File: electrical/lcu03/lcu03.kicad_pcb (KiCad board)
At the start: 2 copper layers, 99.5 x 50 mm, 121 parts, among them P1 screw, P10 swd, P11 stepper_conn, P12 stepper_conn, P13 stepper_conn, P14 stepper_conn, P15 stepper_conn, P16 screw, P17 screw, P2 screw, P3 screw, P4 screw, P5 ext-1, P6 ~rst~, P7 mode, P8 ext-2, P9 USB_B, Q1 bc857, Q2 bc847, Q3 bc857, Q4 ntd18n06l, U1 crystal-4pin, U2 CP2102, U3 m24c02, U4 NCP3063, U5 MCP1703T-3302E/CB, U6 ts881, U7 lb1930mc, U8 a4985, U9 a4985

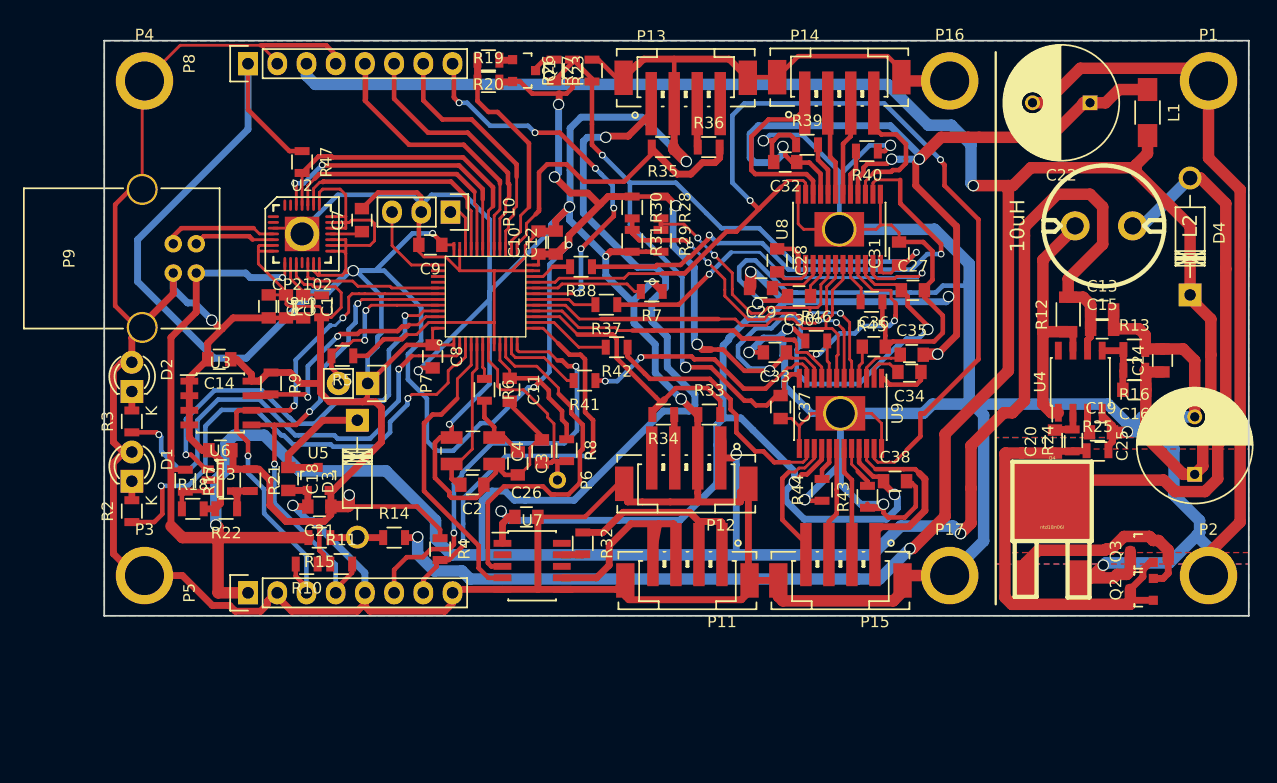
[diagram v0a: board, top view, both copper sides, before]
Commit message: Replaced linear regulator, changed socket footprints and implemented all improvements from "zzz.txt" file.
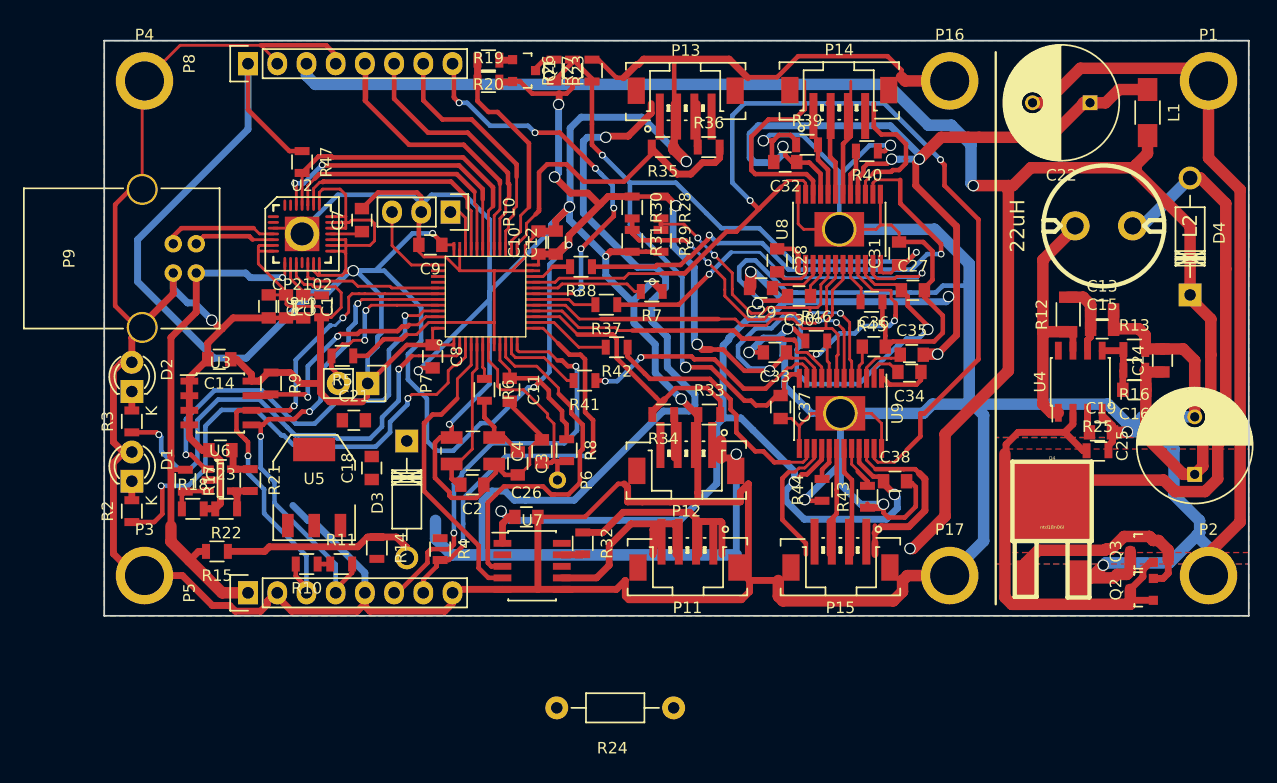
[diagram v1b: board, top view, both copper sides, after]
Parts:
- removed C20: 10n, Capacitors_SMD:C_0805
- C19: value 1n2 -> 2n4
- L2: value 10uH -> 22uH
- P11, P12, P13, P14, P15: footprint my-lib:JST_B4B-PH-SM4-TB -> my-lib:my-JST_B4B-PH-SM4-TB
- R14, R15: value 0 -> ferrite bead
- R24: value 470 5% -> 10 5%; footprint Resistors_SMD:R_0805 -> Resistors_ThroughHole:Resistor_Horizontal_RM10mm
- R32: value 10 5% -> 0
- U5: value MCP1703T-3302E/CB -> my-NCP1117ST50T3G; footprint TO_SOT_Packages_SMD:SOT-23 -> TO_SOT_Packages_SMD:SOT-223
- moved R24 41.7 mm to (137.5, 129.0), turned to 180 degrees
- moved R15 8.98 mm to (97.8, 115.4)
- moved C21 8.08 mm to (109.7, 104.0), turned to 0 degrees
- moved C18 7.31 mm to (111.2, 108.2), turned to 90 degrees
- moved D3 4.66 mm to (114.3, 105.8)
- moved R14 1.75 mm to (111.7, 115.1), turned to 270 degrees
- moved U5 0.83 mm to (106.2, 109.8)
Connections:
- Q2 pad 1: Net-(C20-Pad1) -> Net-(Q2-Pad1)
- Q2 pad 3: Net-(C20-Pad1) -> Net-(Q2-Pad1)
- Q3 pad 1: Net-(C20-Pad1) -> Net-(Q2-Pad1)
- R24 pad 1: Net-(C20-Pad1) -> Net-(P11-Pad1)
- R24 pad 2: Net-(C20-Pad2) -> /shutter-out-a
- R25 pad 1: Net-(C20-Pad1) -> Net-(Q2-Pad1)
- U4 pad 2: Net-(C20-Pad2) -> Net-(Q2-Pad1)
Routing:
- net /Vbus: track 266.3 -> 53.7 mm, vias 5 -> 1
- net GND: track 834.7 -> 936.9 mm, vias 18 -> 19
- net /reg-fb: track 210.2 -> 162.8 mm, vias 3 -> 2
- net VDD: track 373.9 -> 332.8 mm, vias 11 -> 10
- net Net-(Q2-Pad1): track 0.00 -> 41.1 mm
- net Net-(C20-Pad1): track 37.5 -> 0.00 mm
- net Net-(D3-Pad2): track 4.63 -> 17.4 mm
- net Net-(C18-Pad1): track 10.9 -> 0.00 mm
- net Net-(C20-Pad2): track 3.00 -> 0.00 mm
- net /tx-2: track 38.0 -> 37.4 mm

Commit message: Finished routing. Going to apply a few beautifications.
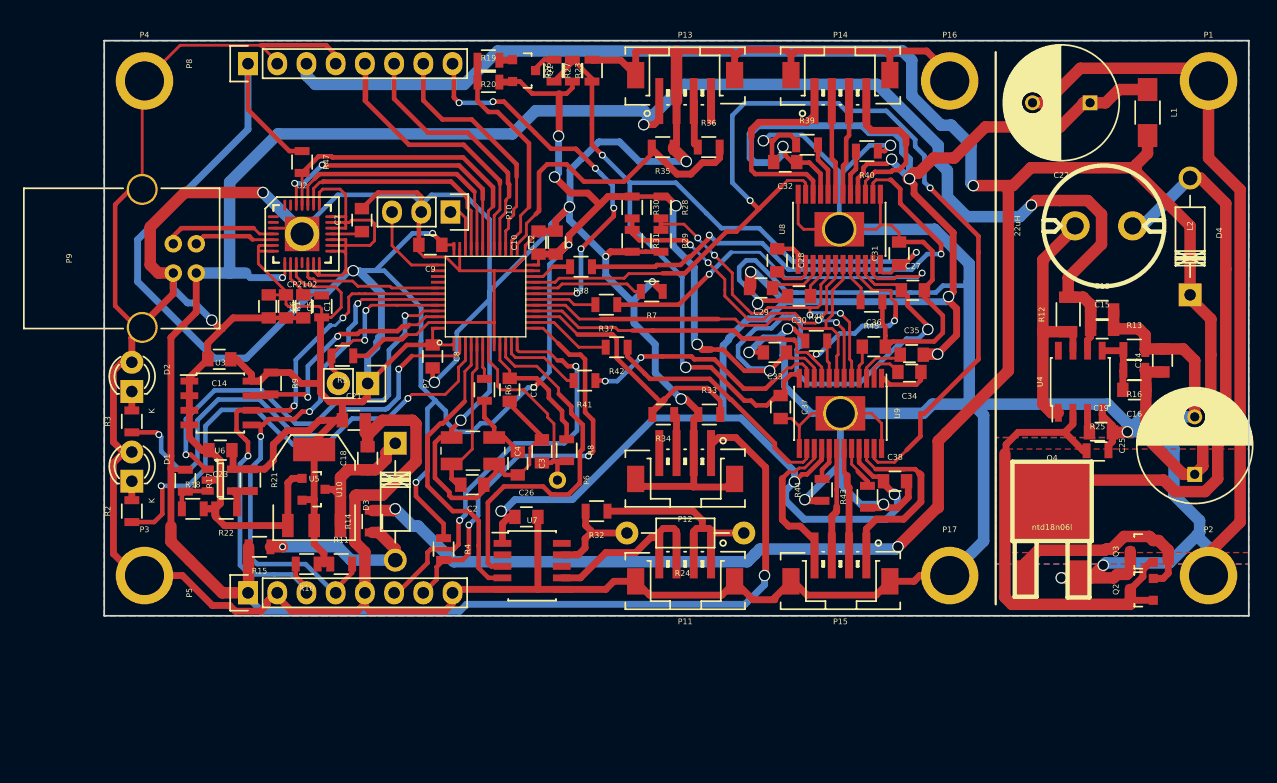
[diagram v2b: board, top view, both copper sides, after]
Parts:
- added U10: MCP1703T-3302E/CB, TO_SOT_Packages_SMD:SOT-23, F.Cu at (106.2, 110.0)
- moved R24 16.4 mm to (143.6, 113.8)
- moved R15 3.72 mm to (101.5, 115.0)
- moved R32 3.05 mm to (130.8, 111.9), turned to 180 degrees
- moved R14 2.33 mm to (111.3, 112.8), turned to 90 degrees
- moved P13 1.35 mm to (138.5, 74.0)
- moved P14 1.30 mm to (152.0, 74.0)
- moved P11 1.22 mm to (138.5, 118.0)
- moved P15 1.20 mm to (152.0, 118.0)
- moved D3 1.02 mm to (113.3, 106.0)
- moved C18 0.92 mm to (110.9, 107.3)
- moved P12 0.71 mm to (138.5, 109.1)
- moved R4 0.30 mm to (117.5, 115.2)
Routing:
- net /Vbus: track 53.7 -> 228.8 mm, vias 1 -> 4
- net GND: track 936.9 -> 859.7 mm
- net /reg-fb: track 162.8 -> 215.4 mm, vias 2 -> 3
- net VDD: track 332.8 -> 381.9 mm, vias 10 -> 11
- net Net-(C18-Pad1): track 0.00 -> 14.6 mm
- net /shutter-out-a: track 1.84 -> 9.00 mm
- net /stepper-subcircuit-2/out1b: track 11.8 -> 16.4 mm
- net /i2c1-sda: track 44.2 -> 47.5 mm
- net /shutter-out-b: track 21.0 -> 18.0 mm
- net /stepper-subcircuit-1/Vbb: track 180.1 -> 177.3 mm
- net /i2c1-scl: track 45.9 -> 48.7 mm
- net /stepper-subcircuit-2/out2a: track 12.1 -> 9.48 mm
- net /stepper-subcircuit-1/out1a: track 10.9 -> 8.32 mm
- net /stepper-subcircuit-2/out2b: track 20.2 -> 17.7 mm
- net Net-(D3-Pad2): track 17.4 -> 14.9 mm, vias 0 -> 1
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
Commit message: Finished beautifications. Generated gerber files.
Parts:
- moved C13 0.55 mm to (174.8, 93.9)
- moved C16 0.35 mm to (177.6, 101.7)
- moved R13 0.25 mm to (177.6, 97.6)
- moved C15 0.16 mm to (174.8, 95.9)
- moved R16 0.07 mm to (177.6, 99.7)
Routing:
- net VDD: track 381.9 -> 406.5 mm, vias 11 -> 10
- net GND: track 859.7 -> 869.6 mm, vias 19 -> 21
- net /Vbus: track 228.8 -> 223.6 mm
- net /stepper-subcircuit-1/Vbb: track 177.3 -> 180.9 mm, vias 9 -> 8
- net /reg-fb: track 215.4 -> 212.0 mm
- net /hall2: track 28.6 -> 25.4 mm
- net /stepper-subcircuit-1/ms2: track 34.4 -> 35.8 mm
- net /stepper-subcircuit-1/ms1: track 32.7 -> 34.1 mm
- net Net-(R37-Pad1): track 35.0 -> 36.1 mm
- net Net-(C16-Pad2): track 5.41 -> 6.23 mm
- net /stepper-subcircuit-1/ref: track 80.7 -> 80.0 mm
- net Net-(R41-Pad1): track 22.4 -> 23.0 mm
- net /hall1: track 24.1 -> 24.6 mm
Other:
- board text removed: "Here use 2n4 instead to decrease frequency down to 150kHz."

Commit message: Changed component value.
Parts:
- C19: value 2n4 -> 2n2
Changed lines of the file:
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@@
     (links 318)
     (no_connects 0)
-    (area 80.524999 62.15 204.999999 123.08876)
+    (area 87.924999 70.924999 187.575001 121.075001)
     (thickness 1.6)
     (drawings 29)
@@
       (effects (font (size 0.5 0.5) (thickness 0.075)))
     )
-    (fp_text value 2n4 (at 0 2.1) (layer F.Fab)
-      (effects (font (size 0.5 0.5) (thickness 0.075)))
-    )
+    (fp_text value 2n2 (at 0 2.1) (layer F.Fab)
+      (effects (font (size 0.5 0.5) (thickness 0.075)))
+    )

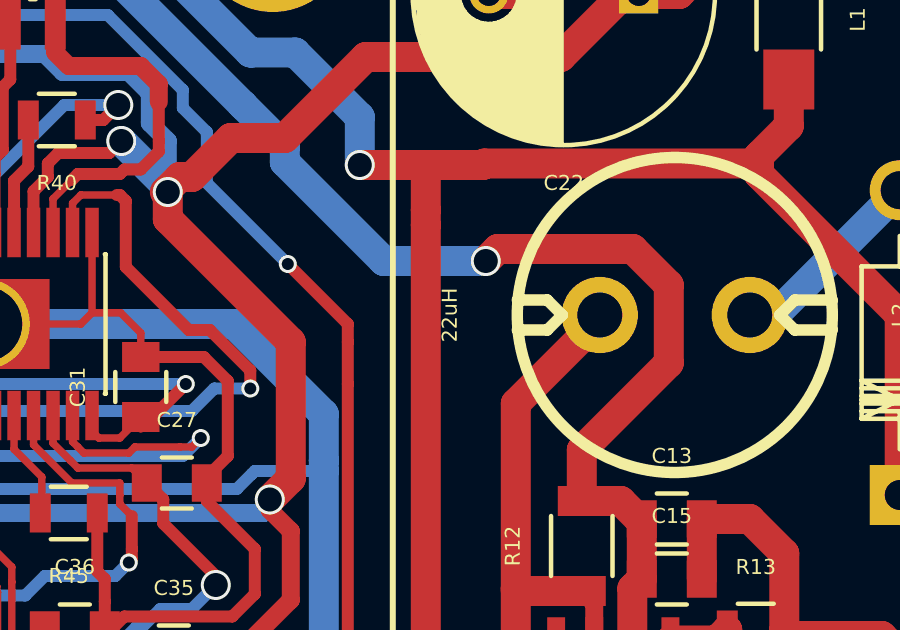
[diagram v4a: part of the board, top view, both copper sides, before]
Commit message: Putting motors in reset mode when not spinning.
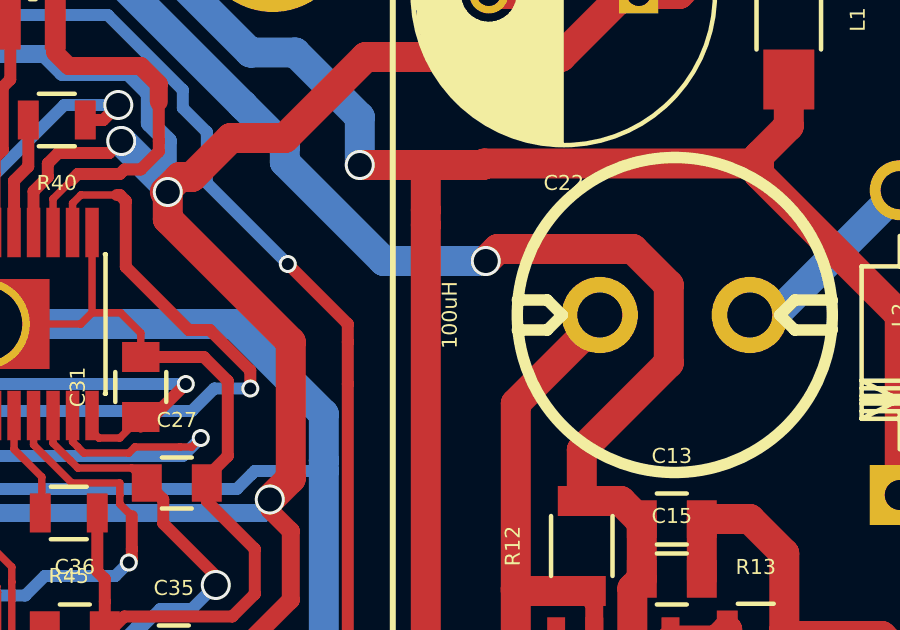
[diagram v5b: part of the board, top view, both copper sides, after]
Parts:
- L2: value 22uH -> 100uH
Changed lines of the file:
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@@
       (effects (font (size 0.5 0.5) (thickness 0.075)))
     )
-    (fp_text value 22uH (at 0 -7.50062 90) (layer F.SilkS)
+    (fp_text value 100uH (at 0 -7.50062 90) (layer F.SilkS)
       (effects (font (size 0.5 0.5) (thickness 0.075)))
     )

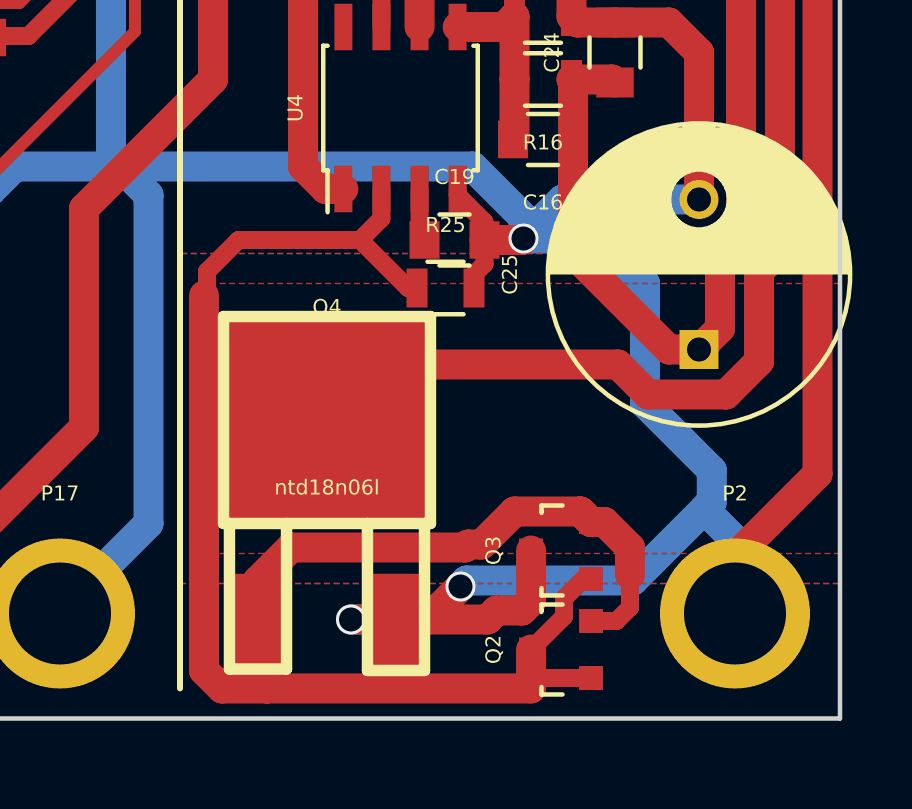
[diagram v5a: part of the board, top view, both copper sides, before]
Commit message: Changed power supply circuit. Removed transistors and introduced 100R resistor in series.
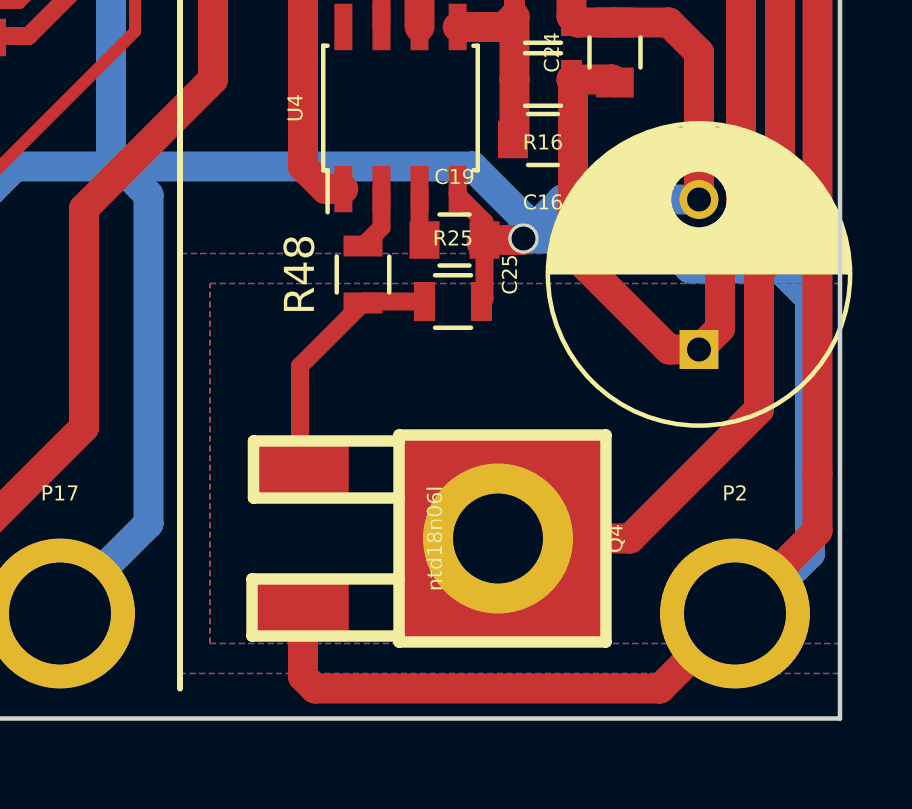
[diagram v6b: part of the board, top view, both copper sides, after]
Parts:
- removed Q2: bc847, TO_SOT_Packages_SMD:SOT-23
- removed Q3: bc857, TO_SOT_Packages_SMD:SOT-23
- added R48: 100 5%, Resistors_SMD:R_0805, F.Cu at (171.6, 106.2)
- moved Q4 2.82 mm to (169.6, 115.0), turned to 270 degrees
- moved R25 0.51 mm to (174.6, 107.1)
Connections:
- Q4 pad 1: Net-(Q2-Pad2) -> Net-(Q4-Pad1)
- R25 pad 1: Net-(Q2-Pad1) -> Net-(Q4-Pad1)
- U4 pad 2: Net-(Q2-Pad1) -> Net-(R48-Pad2)
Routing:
- net Net-(Q2-Pad1): track 41.1 -> 0.00 mm
- net Net-(Q2-Pad2): track 19.1 -> 0.00 mm
- net Net-(Q4-Pad1): track 0.00 -> 8.53 mm
- net Net-(D4-Pad2): track 51.0 -> 46.9 mm
- net Net-(R48-Pad2): track 0.00 -> 2.15 mm
- net GND: track 869.6 -> 870.1 mm, vias 21 -> 19
- added copper zone on B.Cu, net Net-(D4-Pad2)
